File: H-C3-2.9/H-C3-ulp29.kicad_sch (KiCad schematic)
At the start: 61 parts, among them IC101 ESP32-C3-WROOM-02-H4, J1 USB_C_Receptacle_USB2.0, J2 AFC24-S24FIC-00, J3 SM02B-SRSS-TB(LF)(SN), J4 SM04B-SRSS-TB_LF__SN_, J5 OLED, Q1 Si1308, Q2 Si2301CDS, SW1 SW_Push_Dual, SW2 SW_Push_Dual, U2 SGM6029CYG/TR, U3 TP4057-42-SOT26-R, U4 K2-1806SQ-A2DW-04, U5 K2-1806SQ-A2DW-04, U6 K2-1806SQ-A2DW-04, Y1 RV-3032-C7

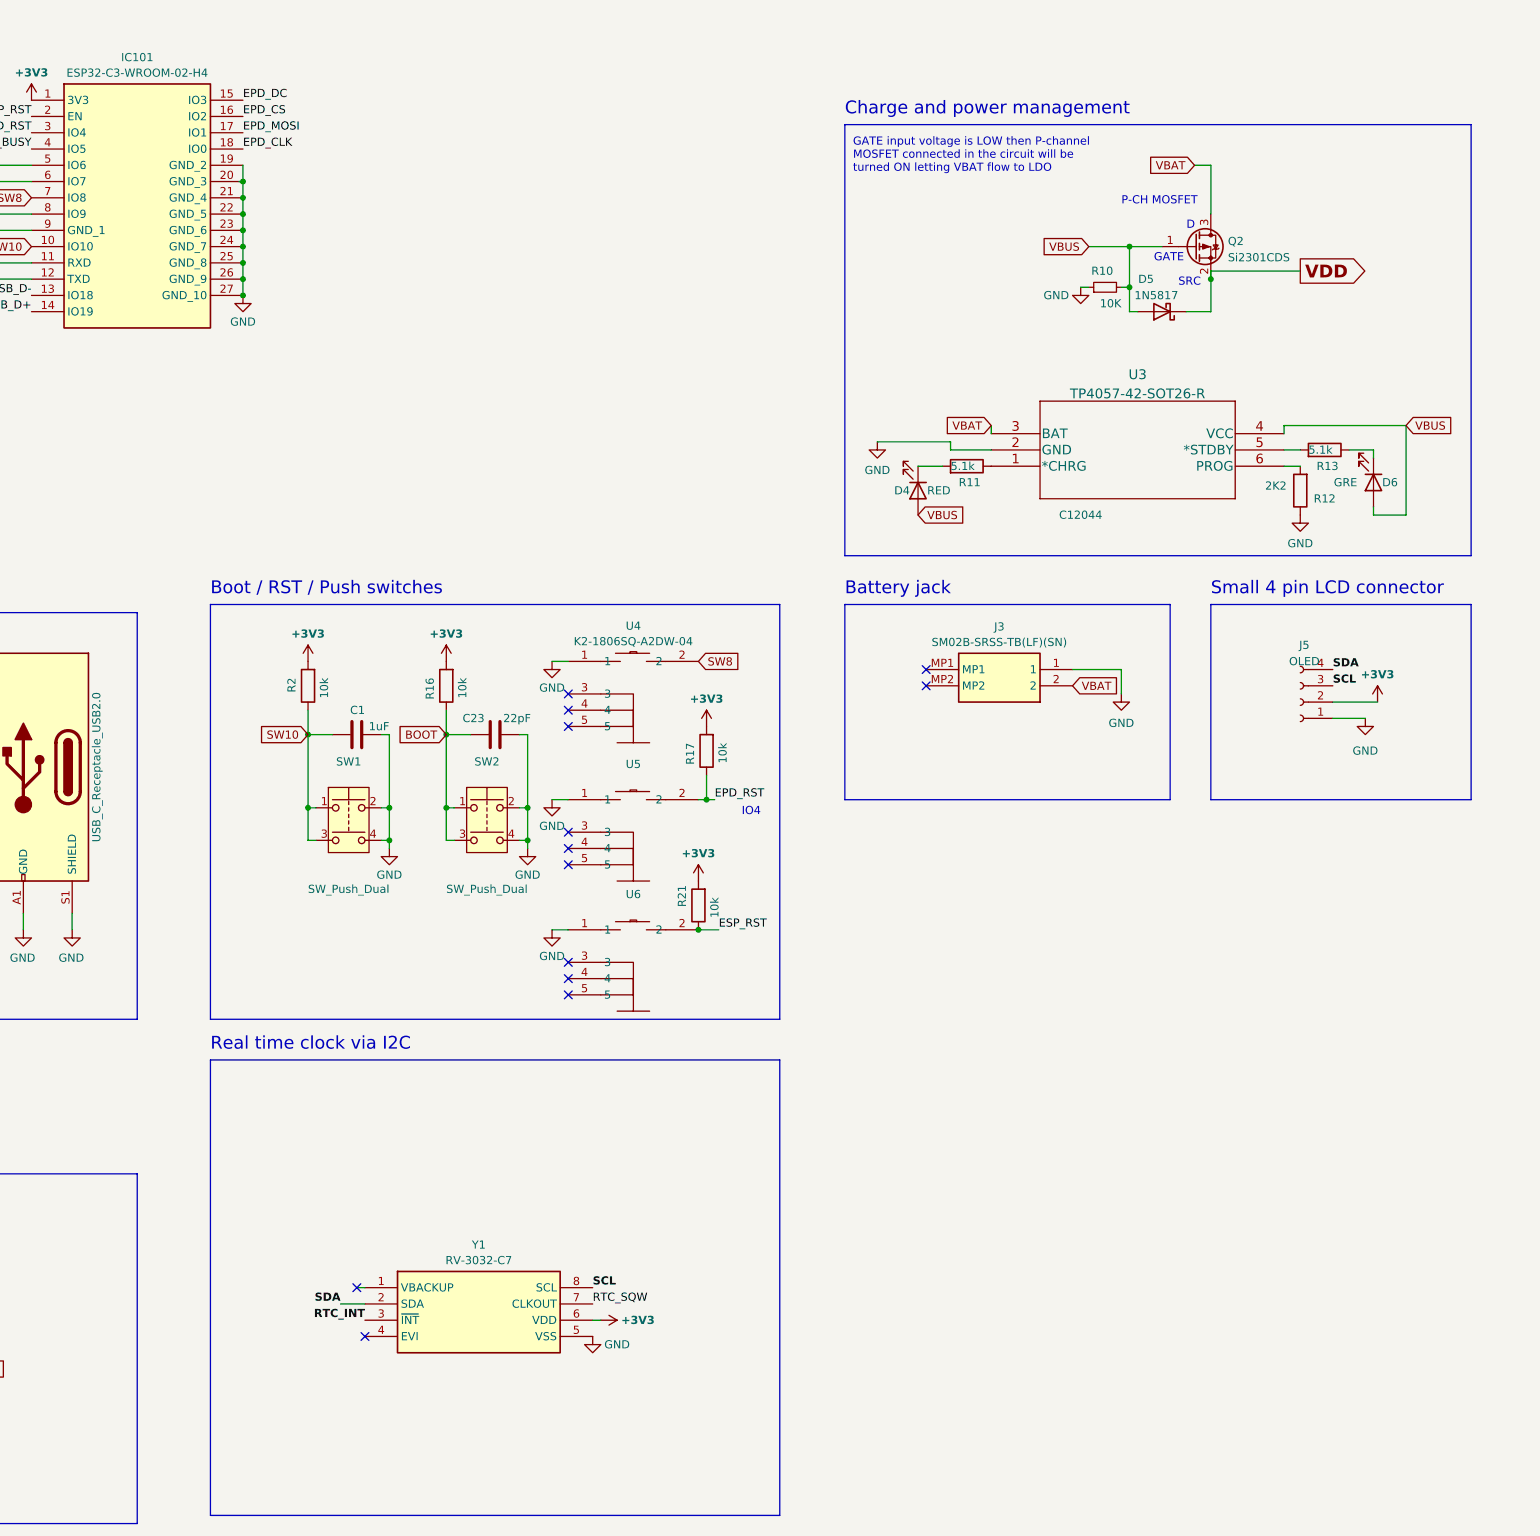
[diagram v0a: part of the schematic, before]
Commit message: Add PCF RTC
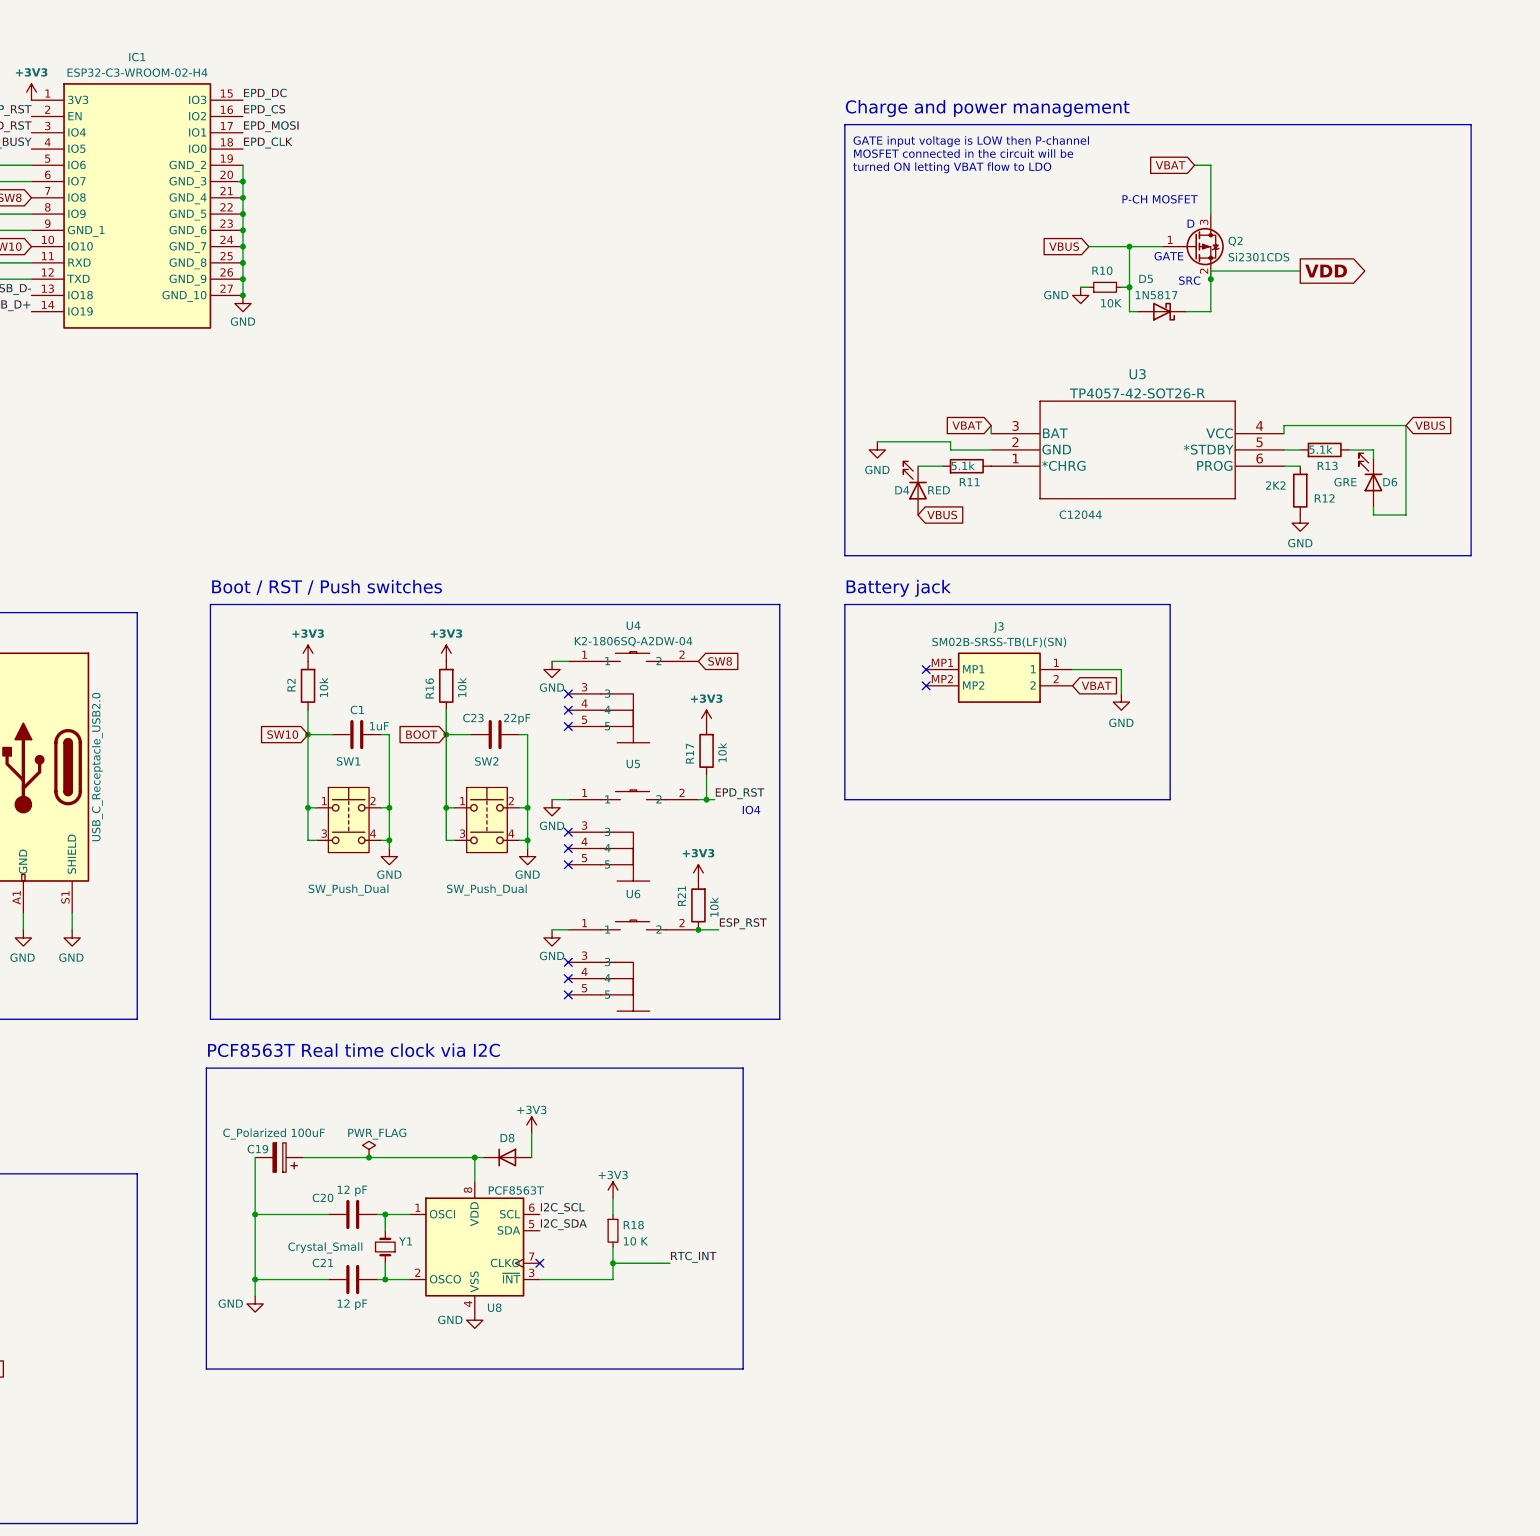
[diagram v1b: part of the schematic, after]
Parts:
- removed J5: OLED, Connector_PinSocket_2.54mm:PinSocket_1x04_P2.54mm_Vertical, symbol Connector:Conn_01x04_Socket
- removed Y1: RV-3032-C7, footprints:RV3032C7, symbol RTC:RV-3032-C7
- added C19: C_Polarized 100uF, Capacitor_Tantalum_SMD:CP_EIA-3528-21_Kemet-B, symbol Device:C_Polarized
- added C20, C21: 12 pF, Capacitor_SMD:C_0603_1608Metric, symbol Device:C
- added D8: 1N4148WS, Diode_SMD:D_SOD-323, symbol Diode:1N4148WS
- added R18: 10 K, Resistor_SMD:R_0603_1608Metric, symbol Device:R_Small
- added U8: PCF8563T, Package_SO:SOIC-8_3.9x4.9mm_P1.27mm, symbol Timer_RTC:PCF8563T
- added Y1: Crystal_Small, footprints:Q13FC1350000400-Crystal, symbol Device:Crystal_Small
- renumbered IC101 to IC1
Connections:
- net +3V3: now also D8.2 (A), R18.1
- net GND: now also C19.2, C20.1, C21.1, U8.4 (VSS)
- net RTC_INT: now also R18.2, U8.3 (~{INT})
- new net: C21.2, U8.2 (OSCO), Y1.1
- new net: C20.2, U8.1 (OSCI), Y1.2
- new net: C19.1, D8.1 (K), U8.8 (VDD)
- new net I2C_SCL: U8.6 (SCL)
- new net I2C_SDA: U8.5 (SDA)
- no-connect marks 18 -> 17
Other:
- note added: "PCF8563T Real time clock via I2C"
- note removed: "Real time clock via I2C"
- note removed: "Small 4 pin LCD connector"

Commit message: Layout 1.0
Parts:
- removed C2, C3: 10 uF, Capacitor_SMD:C_0603_1608Metric, symbol Device:C
- removed L2: 0.47 uH, footprints:IND-SMD_L2.5-W2.0_SPH252012, symbol Device:L
- removed R3: 249k 1%, Resistor_SMD:R_0603_1608Metric, symbol Device:R
- removed U2: SGM6029CYG/TR, footprints:SGM6029_WLCSP-6, symbol SGM:SGM6029CYG_TR
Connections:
- net +3V3: now also J4.2; no longer J4.3
- net GND: now also J4.1; no longer J4.4
- net SCL: now also J4.4; no longer J4.1
- net SDA: now also J4.3; no longer J4.2
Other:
- note removed: "Buck converter 5V or VBAT to 3V3"
- moved on the sheet: J4

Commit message: Schematics updated. All parts on board
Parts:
- removed C23: 22pF, Capacitor_SMD:C_0402_1005Metric, symbol Device:C
- removed D4: RED, LED_SMD:LED_0805_2012Metric, symbol Device:LED
- removed D6: GRE, LED_SMD:LED_0805_2012Metric, symbol Device:LED
- removed H1: MountingHole, MountingHole:MountingHole_3.7mm, symbol Mechanical:MountingHole
- removed J3: SM02B-SRSS-TB(LF)(SN), footprints:SM02BSRSSTBLFSN, symbol BATTERY:S2B-PH-SM4-TB_LF__SN_
- removed R11, R13: 5.1k, Resistor_SMD:R_0603_1608Metric, symbol Device:R
- removed R12: 2K2, Resistor_SMD:R_0805_2012Metric, symbol Device:R
- removed R16, R17: 10k, Resistor_SMD:R_0402_1005Metric, symbol Device:R
- removed SW1, SW2: SW_Push_Dual, footprints:switch_SKSVCCE010, symbol Switch:SW_Push_Dual
- removed U3: TP4057-42-SOT26-R, footprints:TP4057-42-SOT26-R, symbol TP4057:TP4057-42-SOT26-R
- removed U4, U5: K2-1806SQ-A2DW-04, footprints:KEY-SMD_K2-1806SQ-A3DW-04, symbol easyeda:K2-1806SQ-A2DW-04
- added BT1: Battery_Cell, footprints:BAT-SMD_BS-24-B4AA016, symbol Device:Battery_Cell
- added C2: 22pF, Capacitor_SMD:C_0402_1005Metric, symbol Device:C
- added R3, R4: 10k, Resistor_SMD:R_0402_1005Metric, symbol Device:R
- added SW1, SW2: K2-1806SQ-A2DW-04, footprints:KEY-SMD_K2-1806SQ-A3DW-04, symbol easyeda:K2-1806SQ-A2DW-04
- added TP6: IO8, TestPoint:TestPoint_Pad_D1.0mm, symbol Connector:TestPoint
- renumbered U6 to SW3
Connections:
- net VDD is gone; now on net +3V3: D5.1 (K), Q2.2 (S)
- net VDD33 is gone; now on net +3V3: C9.2, J2.10, J2.9
- net +3V3: now also R3.2, R4.2
- net BOOT: now also C2.1, R4.1, SW1.1
- net EPD_RST: now also R3.1
- net GND: now also BT1.2 (-), C2.2, SW1.2, SW2.2
- net SW10: now also SW2.1; no longer C1.2
- net SW8: no longer names the net of IC1.7 (IO8)
- net SW8: now also TP6.1
- net VBAT renamed +VBAT
- net +VBAT: now also BT1.1 (+)
- no-connect marks 17 -> 9
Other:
- note added: "CR2450 and power management"
- note added: "Open source Mark"
- note removed: "Battery jack"
- note removed: "Charge and power management"
- note removed: "IO4"
- note removed: "Mounting"
- moved on the sheet: D5, J1, J4, Q2, R1, R10, R2, R20, R21, SW3

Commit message: Going forward
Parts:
- removed IC1: ESP32-C3-WROOM-02-H4, ESP32C3WROOM02H4, symbol ESPC3:ESP32-C3-WROOM-02-H4
- removed TP4: IO20, TestPoint:TestPoint_Pad_D1.0mm, symbol Connector:TestPoint
- removed TP5: IO21, TestPoint:TestPoint_Pad_D1.0mm, symbol Connector:TestPoint
- removed TP6: IO8, TestPoint:TestPoint_Pad_D1.0mm, symbol Connector:TestPoint
- added C3, C4: 1uF, Capacitor_SMD:C_0805_2012Metric, symbol Device:C
- added C5: 100nF, Capacitor_SMD:C_0805_2012Metric, symbol Device:C
- added U1: E104-BT5032A, footprints:nRF52832_E104-BT5032A_BYT, symbol Nordic:E104-BT5032A
- added U2: XC6206PxxxMR, Package_TO_SOT_SMD:SOT-23-3, symbol Regulator_Linear:XC6206PxxxMR
- added U3: CH340C, Package_SO:SOIC-16_3.9x9.9mm_P1.27mm, symbol Interface_USB:CH340C
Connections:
- net +3V3: now also U1.17 (VCC)
- net GND: now also C3.1, C4.1, C5.1, U1.1 (GND), U1.16 (GND), U1.9 (GND), U2.1 (GND), U3.1 (GND)
- net USB_D+: now also U3.5 (UD+)
- net USB_D-: now also U3.6 (UD-)
- net +VBAT: no longer names the net of BT1.1 (+), Q2.3 (D)
- net ESP_RST renamed MCU_RST
- net SW10 renamed SW2
- net SW2: now also U1.2 (P0.25)
- net VBUS renamed +5V
- net +5V: now also C3.2, U2.3 (VI)
- new net UART_3.3V: C4.2, C5.2, U2.2 (VO), U3.16 (VCC), U3.4 (V3)
- new net USB_RXD: U1.19 (TXD), U3.3 (RXD)
- new net USB_TXD: U1.18 (RXD), U3.2 (TXD)
- new net ~{CTS}: U1.21 (CTS), U3.9 (~{CTS})
- new net ~{RTS}: U1.20 (RTS), U3.14 (~{RTS})
- no-connect marks 9 -> 13
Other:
- note added: "Ebyte nRF52832 BLE5.0 MCU"
- note added: "USB to UART"
- note removed: "Open source Mark"
- moved on the sheet: BT1, C1, C10, C11, C12, C13, C14, C15, C16, C17, C19, C2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
